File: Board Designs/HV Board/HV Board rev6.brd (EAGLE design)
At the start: 147.4 x 71.4 mm, 63 parts, among them IC1 OKI-78SR, IC2 NE5532SOIC

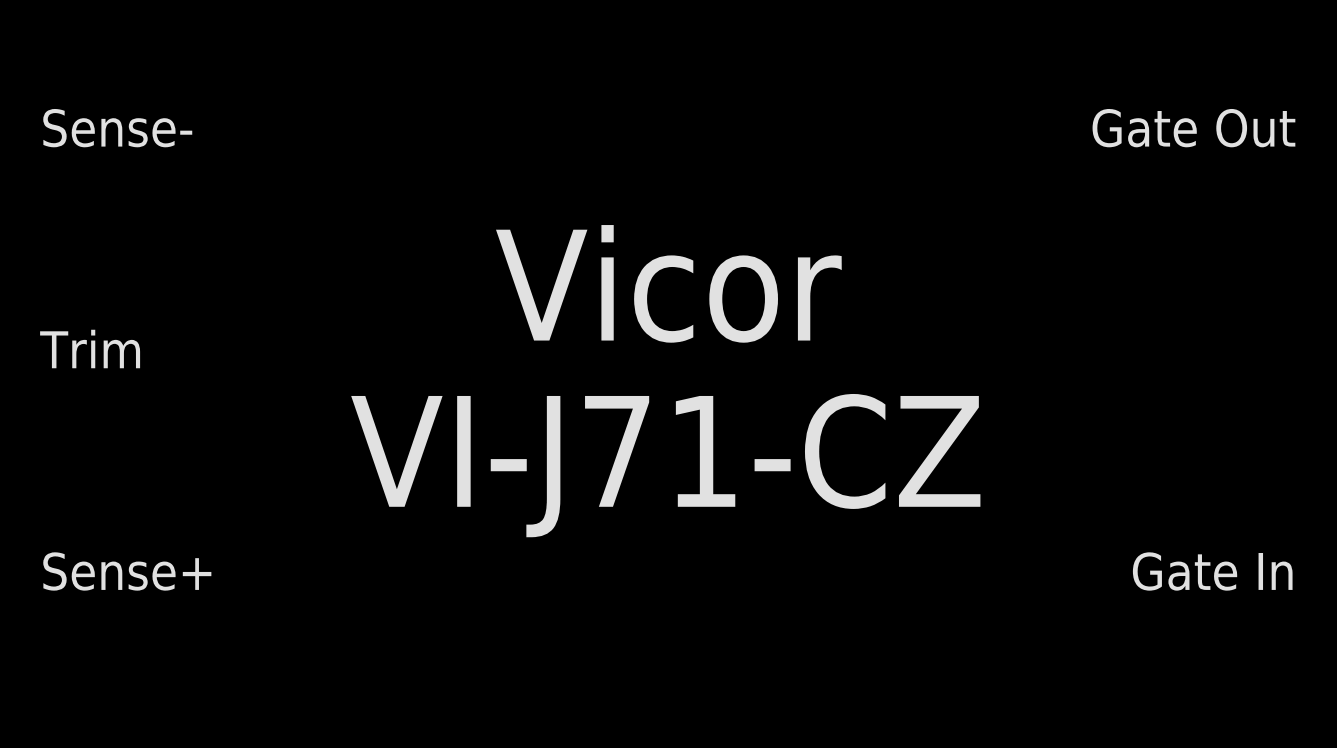
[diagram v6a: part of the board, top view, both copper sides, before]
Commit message: Minor silkscreen updates to HV board rev{6,7}, Update DC/DC converter package to use smaller silkscreen text size, Adjust heatsink pads in Main ECU rev2
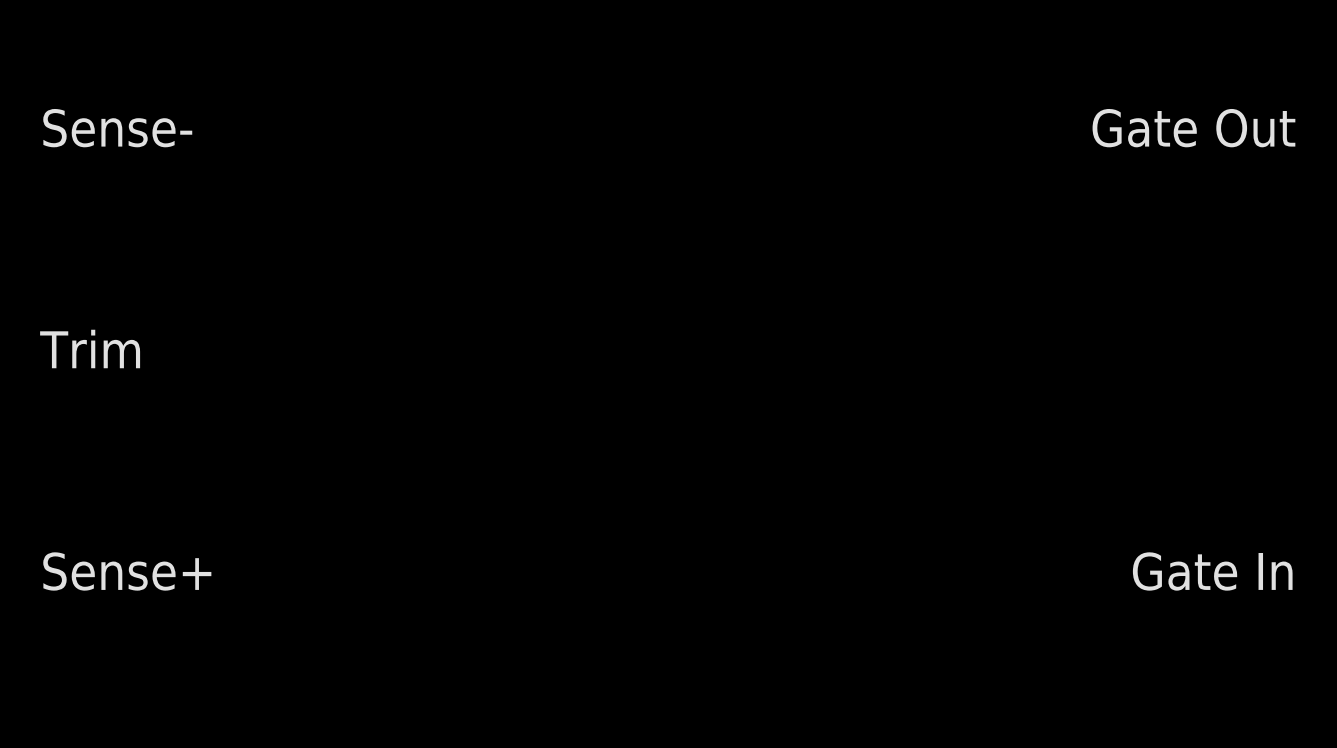
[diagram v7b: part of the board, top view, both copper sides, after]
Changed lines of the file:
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@@
 <plain>
 <wire x1="0" y1="0" x2="147.447" y2="0" width="0" layer="20"/>
-<wire x1="62.611" y1="70.485" x2="62.611" y2="1.016" width="0.8128" layer="51"/>
+<wire x1="62.611" y1="70.739" x2="62.611" y2="0.508" width="0.8128" layer="51"/>
 <text x="61.849" y="20.955" size="2.1844" layer="51" rot="R90">GLV</text>
 <text x="63.627" y="21.717" size="2.1844" layer="51" rot="R270" align="bottom-right">TS</text>
-<wire x1="62.611" y1="70.485" x2="62.611" y2="0.889" width="0.8128" layer="52"/>
+<wire x1="62.611" y1="70.739" x2="62.611" y2="0.508" width="0.8128" layer="52"/>
 <text x="61.849" y="26.797" size="2.1844" layer="52" rot="MR270">GLV</text>
 <text x="63.627" y="25.781" size="2.1844" layer="52" rot="MR90" align="bottom-right">TS</text>
@@
 <text x="82.1436" y="3.302" size="1.397" layer="51" font="vector" align="bottom-center">TRACTIVE SYSTEM
 PCB AREA</text>
-<wire x1="135.382" y1="71.374" x2="135.382" y2="60.833" width="0.8128" layer="52"/>
+<wire x1="135.382" y1="70.866" x2="135.382" y2="60.833" width="0.8128" layer="52"/>
 <wire x1="135.382" y1="60.833" x2="130.81" y2="56.261" width="0.8128" layer="52"/>
 <wire x1="130.81" y1="56.261" x2="130.81" y2="12.319" width="0.8128" layer="52"/>
 <wire x1="130.81" y1="12.319" x2="135.89" y2="7.239" width="0.8128" layer="52"/>
 <wire x1="135.89" y1="7.239" x2="135.89" y2="0.508" width="0.8128" layer="52"/>
-<wire x1="135.382" y1="71.374" x2="135.382" y2="61.087" width="0.8128" layer="51"/>
+<wire x1="135.382" y1="70.866" x2="135.382" y2="61.087" width="0.8128" layer="51"/>
 <wire x1="135.382" y1="60.833" x2="130.81" y2="56.261" width="0.8128" layer="51"/>
 <wire x1="130.81" y1="56.261" x2="130.81" y2="12.319" width="0.8128" layer="51"/>
@@
 <attribute name="VALUE" x="25.527" y="45.466" size="0.6096" layer="28" rot="MR90" align="bottom-center"/>
 </element>
-<element name="U$5" library="HyTechDevices" package="HV_DCDC_VI-J71-CZ" value="HV_DCDC_VI-J71-CZ" x="98.806" y="9.652" smashed="yes" rot="R180"/>
+<element name="U$5" library="HyTechDevices" package="HV_DCDC_VI-J71-CZ" value="HV_DCDC_VI-J71-CZ" x="98.806" y="9.652" smashed="yes" rot="R180">
+<attribute name="VALUE" x="81.026" y="39.878" size="2.032" layer="28" align="center"/>
+</element>
 <element name="INTERLOCK" library="HyTechDevices" package="NANO-FIT_VERTICAL-2" value="INTERLOCK" x="29.21" y="35.052" smashed="yes">
 <attribute name="VALUE" x="29.591" y="37.211" size="0.8128" layer="27" align="bottom-center"/>
